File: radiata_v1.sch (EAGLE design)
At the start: 91 parts, among them IC1 TINY24/44/84-SSU, IC2 MEGA48/88/168-AU

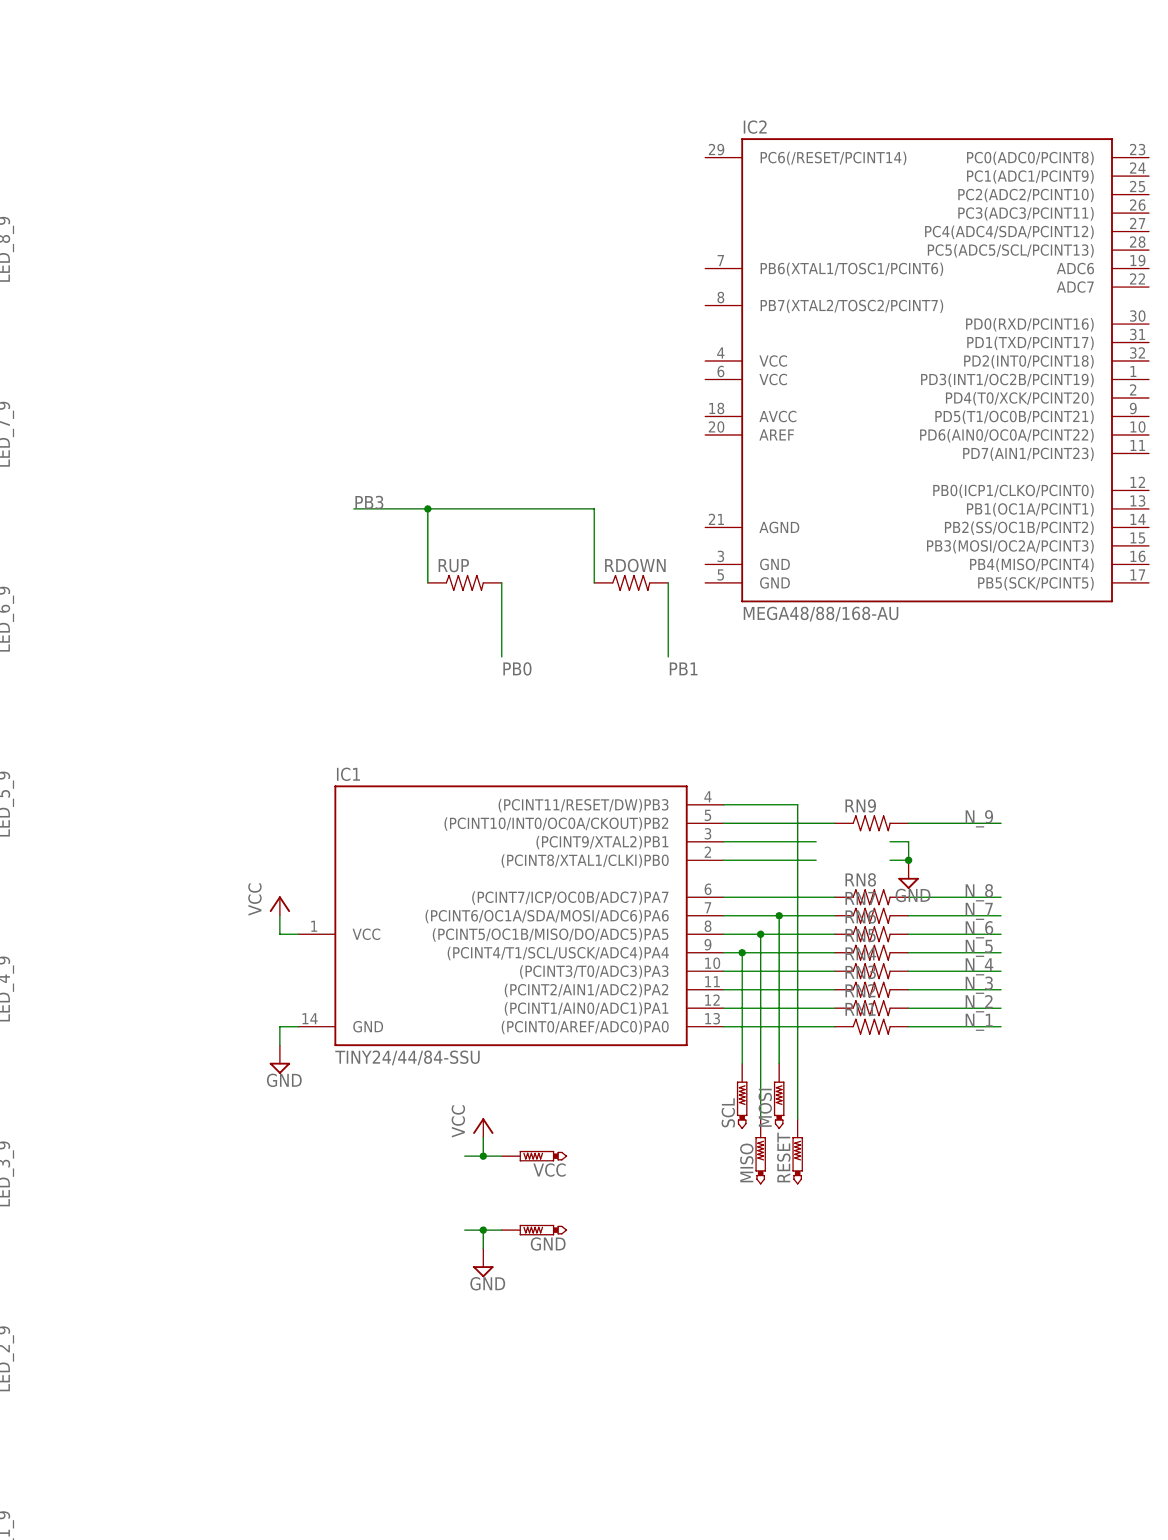
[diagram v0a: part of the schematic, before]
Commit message: rename simpleclock to 'radiata'
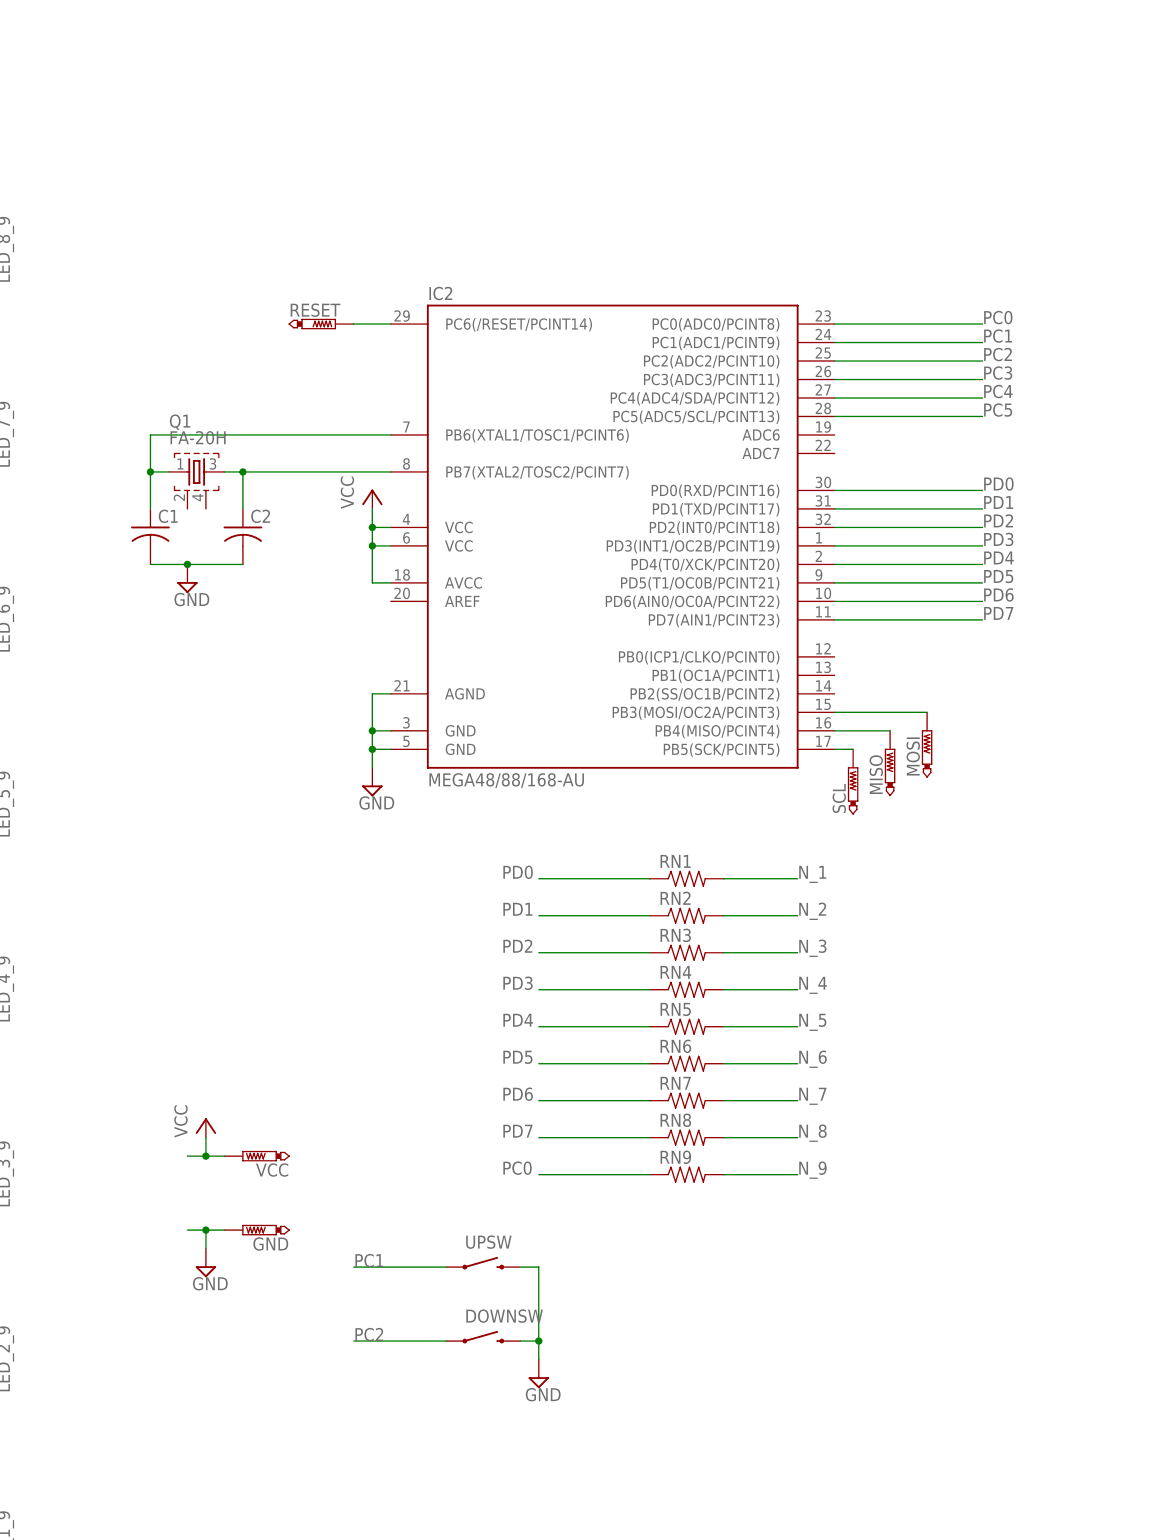
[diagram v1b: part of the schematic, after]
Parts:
- removed IC1: TINY24/44/84-SSU, avr-7:TINY24/44/84-SSU
- removed RDOWN, RUP: (no value), SparkFun:RESISTOR1206
- added C1, C2: (no value), rcl:C-USC0603
- added DOWNSW, UPSW: SWITCH-MOMENTARY-2, SparkFun:SWITCH-MOMENTARY-2
- added Q1: FA-20H, crystal:FA-20H
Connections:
- removed net PA0: IC1.(PCINT0/AREF/ADC0)PA0, RN1.1
- removed net PA1: IC1.(PCINT1/AIN0/ADC1)PA1, RN2.1
- removed net PA2: IC1.(PCINT2/AIN1/ADC2)PA2, RN3.1
- removed net PA3: IC1.(PCINT3/T0/ADC3)PA3, RN4.1
- removed net PA4: IC1.(PCINT4/T1/SCL/USCK/ADC4)PA4, RN5.1, SCL.TP
- removed net PA5: IC1.(PCINT5/OC1B/MISO/DO/ADC5)PA5, MISO.TP, RN6.1
- removed net PA6: IC1.(PCINT6/OC1A/SDA/MOSI/ADC6)PA6, MOSI.TP, RN7.1
- removed net PA7: IC1.(PCINT7/ICP/OC0B/ADC7)PA7, RN8.1
- removed net PB2: IC1.(PCINT10/INT0/OC0A/CKOUT)PB2, RN9.1
- removed net PB3: IC1.(PCINT11/RESET/DW)PB3, RDOWN.1, RESET.TP, RUP.1
- new net N$5: IC2.PC6(/RESET/PCINT14), RESET.TP
- new net N$6: IC2.PB5(SCK/PCINT5), SCL.TP
- new net N$7: IC2.PB4(MISO/PCINT4), MISO.TP
- new net N$8: IC2.PB3(MOSI/OC2A/PCINT3), MOSI.TP
- new net PC0: IC2.PC0(ADC0/PCINT8), RN9.1
- new net PC1: IC2.PC1(ADC1/PCINT9), UPSW.1
- new net PC2: DOWNSW.1, IC2.PC2(ADC2/PCINT10)
- new net PC3: IC2.PC3(ADC3/PCINT11)
- new net PC4: IC2.PC4(ADC4/SDA/PCINT12)
- new net PC5: IC2.PC5(ADC5/SCL/PCINT13)
- new net PD0: IC2.PD0(RXD/PCINT16), RN1.1
- new net PD1: IC2.PD1(TXD/PCINT17), RN2.1
- new net PD2: IC2.PD2(INT0/PCINT18), RN3.1
- new net PD3: IC2.PD3(INT1/OC2B/PCINT19), RN4.1
- new net PD4: IC2.PD4(T0/XCK/PCINT20), RN5.1
- new net PD5: IC2.PD5(T1/OC0B/PCINT21), RN6.1
- new net PD6: IC2.PD6(AIN0/OC0A/PCINT22), RN7.1
- new net PD7: IC2.PD7(AIN1/PCINT23), RN8.1
- net GND: now also C1.2, C2.2, DOWNSW.2, IC2.AGND, IC2.GND@1, IC2.GND@2, UPSW.2; no longer IC1.GND
- net PB0: now also C2.1, IC2.PB7(XTAL2/TOSC2/PCINT7), Q1.3; no longer IC1.(PCINT8/XTAL1/CLKI)PB0, RUP.2
- net PB1: now also C1.1, IC2.PB6(XTAL1/TOSC1/PCINT6), Q1.1; no longer IC1.(PCINT9/XTAL2)PB1, RDOWN.2
- net VCC: now also IC2.AVCC, IC2.VCC@1, IC2.VCC@2; no longer IC1.VCC
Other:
- moved on the sheet: GND, IC2, MISO, MOSI, RESET, RN1, RN2, RN3, RN4, RN5, RN6, RN7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

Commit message: lots of progress, driving towards a scroll wheel that passes DRC
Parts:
- added GND2, V+: PTR1TP20SQ, testpad:PTR1TP20SQ
- added RR1, RR2, RR3, RS1, RS2, RS3: (no value), SparkFun:RESISTOR1206
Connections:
- new net ROTOR1: RR1.1, RS1.2
- new net ROTOR2: RR2.1, RS2.2
- new net ROTOR3: RR3.1, RS3.2
- net GND: now also GND2.TP
- net PC2: now also RS1.1, RS2.1, RS3.1
- net PC3: now also RR1.2
- net PC4: now also RR2.2
- net PC5: now also RR3.2
- net VCC: now also V+.TP
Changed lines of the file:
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@@
 <part name="DOWNSW" library="SparkFun" deviceset="SWITCH-MOMENTARY-2" device=""/>
 <part name="SUPPLY5" library="supply2" deviceset="GND" device=""/>
+<part name="RS1" library="SparkFun" deviceset="RESISTOR" device="1206"/>
+<part name="RS2" library="SparkFun" deviceset="RESISTOR" device="1206"/>
+<part name="RS3" library="SparkFun" deviceset="RESISTOR" device="1206"/>
+<part name="RR1" library="SparkFun" deviceset="RESISTOR" device="1206"/>
+<part name="RR2" library="SparkFun" deviceset="RESISTOR" device="1206"/>
+<part name="RR3" library="SparkFun" deviceset="RESISTOR" device="1206"/>
+<part name="GND2" library="testpad" deviceset="PTR1" device="TP20SQ"/>
+<part name="V+" library="testpad" deviceset="PTR1" device="TP20SQ"/>
 </parts>
 <sheets>
@@
 </instance>
 <instance part="SUPPLY5" gate="GND" x="304.8" y="48.26"/>
+<instance part="RS1" gate="G$1" x="299.72" y="30.48"/>
+<instance part="RS2" gate="G$1" x="299.72" y="22.86"/>
+<instance part="RS3" gate="G$1" x="299.72" y="15.24"/>
+<instance part="RR1" gate="G$1" x="317.5" y="30.48"/>
+<instance part="RR2" gate="G$1" x="317.5" y="22.86"/>
+<instance part="RR3" gate="G$1" x="317.5" y="15.24"/>
+<instance part="GND2" gate="G$1" x="254" y="68.58" rot="R270"/>
+<instance part="V+" gate="G$1" x="254" y="78.74" rot="R270"/>
 </instances>
 <busses>
@@
 <wire x1="256.54" y1="78.74" x2="259.08" y2="78.74" width="0.1524" layer="91"/>
 <junction x="259.08" y="78.74"/>
+<pinref part="V+" gate="G$1" pin="TP"/>
 </segment>
 <segment>
@@
 <wire x1="259.08" y1="66.04" x2="259.08" y2="68.58" width="0.1524" layer="91"/>
 <junction x="259.08" y="68.58"/>
+<pinref part="GND2" gate="G$1" pin="TP"/>
 </segment>
 <segment>
@@
 <label x="279.4" y="53.34" size="1.778" layer="95"/>
 </segment>
+<segment>
+<pinref part="RS3" gate="G$1" pin="1"/>
+<wire x1="294.64" y1="15.24" x2="292.1" y2="15.24" width="0.1524" layer="91"/>
+<wire x1="292.1" y1="15.24" x2="292.1" y2="22.86" width="0.1524" layer="91"/>
+<wire x1="292.1" y1="22.86" x2="292.1" y2="30.48" width="0.1524" layer="91"/>
+<wire x1="292.1" y1="30.48" x2="279.4" y2="30.48" width="0.1524" layer="91"/>
+<pinref part="RS1" gate="G$1" pin="1"/>
+<wire x1="294.64" y1="30.48" x2="292.1" y2="30.48" width="0.1524" layer="91"/>
+<junction x="292.1" y="30.48"/>
+<pinref part="RS2" gate="G$1" pin="1"/>
+<wire x1="294.64" y1="22.86" x2="292.1" y2="22.86" width="0.1524" layer="91"/>
+<junction x="292.1" y="22.86"/>
+<label x="279.4" y="30.48" size="1.778" layer="95"/>
+</segment>
 </net>
 <net name="PC3" class="0">
@@
 <label x="365.76" y="185.42" size="1.778" layer="95"/>
 </segment>
+<segment>
+<pinref part="RR1" gate="G$1" pin="2"/>
+<wire x1="332.74" y1="30.48" x2="322.58" y2="30.48" width="0.1524" layer="91"/>
+<label x="332.74" y="30.48" size="1.778" layer="95"/>
+</segment>
 </net>
 <net name="PC4" class="0">
@@
 <label x="365.76" y="182.88" size="1.778" layer="95"/>
 </segment>
+<segment>
+<pinref part="RR2" gate="G$1" pin="2"/>
+<wire x1="332.74" y1="22.86" x2="322.58" y2="22.86" width="0.1524" layer="91"/>
+<label x="332.74" y="22.86" size="1.778" layer="95"/>
+</segment>
 </net>
 <net name="PC5" class="0">
@@
 <label x="365.76" y="180.34" size="1.778" layer="95"/>
 </segment>
-</net>
+<segment>
+<pinref part="RR3" gate="G$1" pin="2"/>
+<wire x1="332.74" y1="15.24" x2="322.58" y2="15.24" width="0.1524" layer="91"/>
+<label x="332.74" y="15.24" size="1.778" layer="95"/>
+</segment>
+</net>
+<net name="ROTOR1" class="0">
+<segment>
+<pinref part="RS1" gate="G$1" pin="2"/>
+<pinref part="RR1" gate="G$1" pin="1"/>
+<wire x1="304.8" y1="30.48" x2="312.42" y2="30.48" width="0.1524" layer="91"/>
+<label x="302.26" y="33.02" size="1.778" layer="95"/>
+</segment>
+</net>
+<net name="ROTOR2" class="0">
+<segment>
+<pinref part="RS2" gate="G$1" pin="2"/>
+<pinref part="RR2" gate="G$1" pin="1"/>
+<wire x1="304.8" y1="22.86" x2="312.42" y2="22.86" width="0.1524" layer="91"/>
+<label x="302.26" y="25.4" size="1.778" layer="95"/>
+</segment>
+</net>
+<net name="ROTOR3" class="0">
+<segment>
+<pinref part="RS3" gate="G$1" pin="2"/>
+<pinref part="RR3" gate="G$1" pin="1"/>
+<wire x1="304.8" y1="15.24" x2="312.42" y2="15.24" width="0.1524" layer="91"/>
+<label x="302.26" y="17.78" size="1.778" layer="95"/>
+</segment>
+</net>

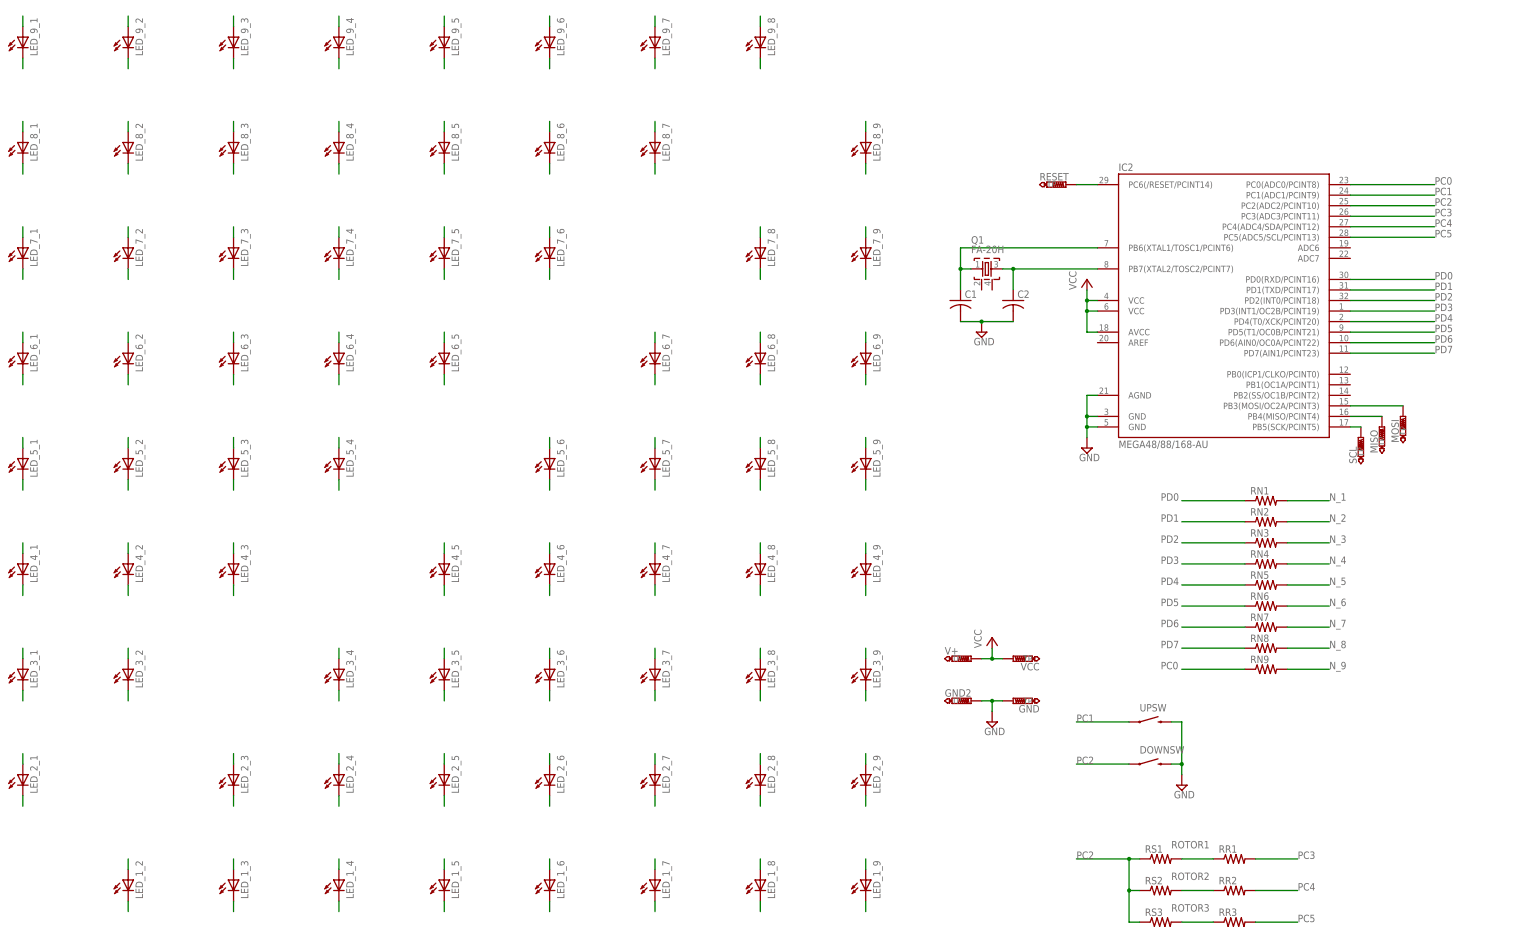
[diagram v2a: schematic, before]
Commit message: add push/pull resistors
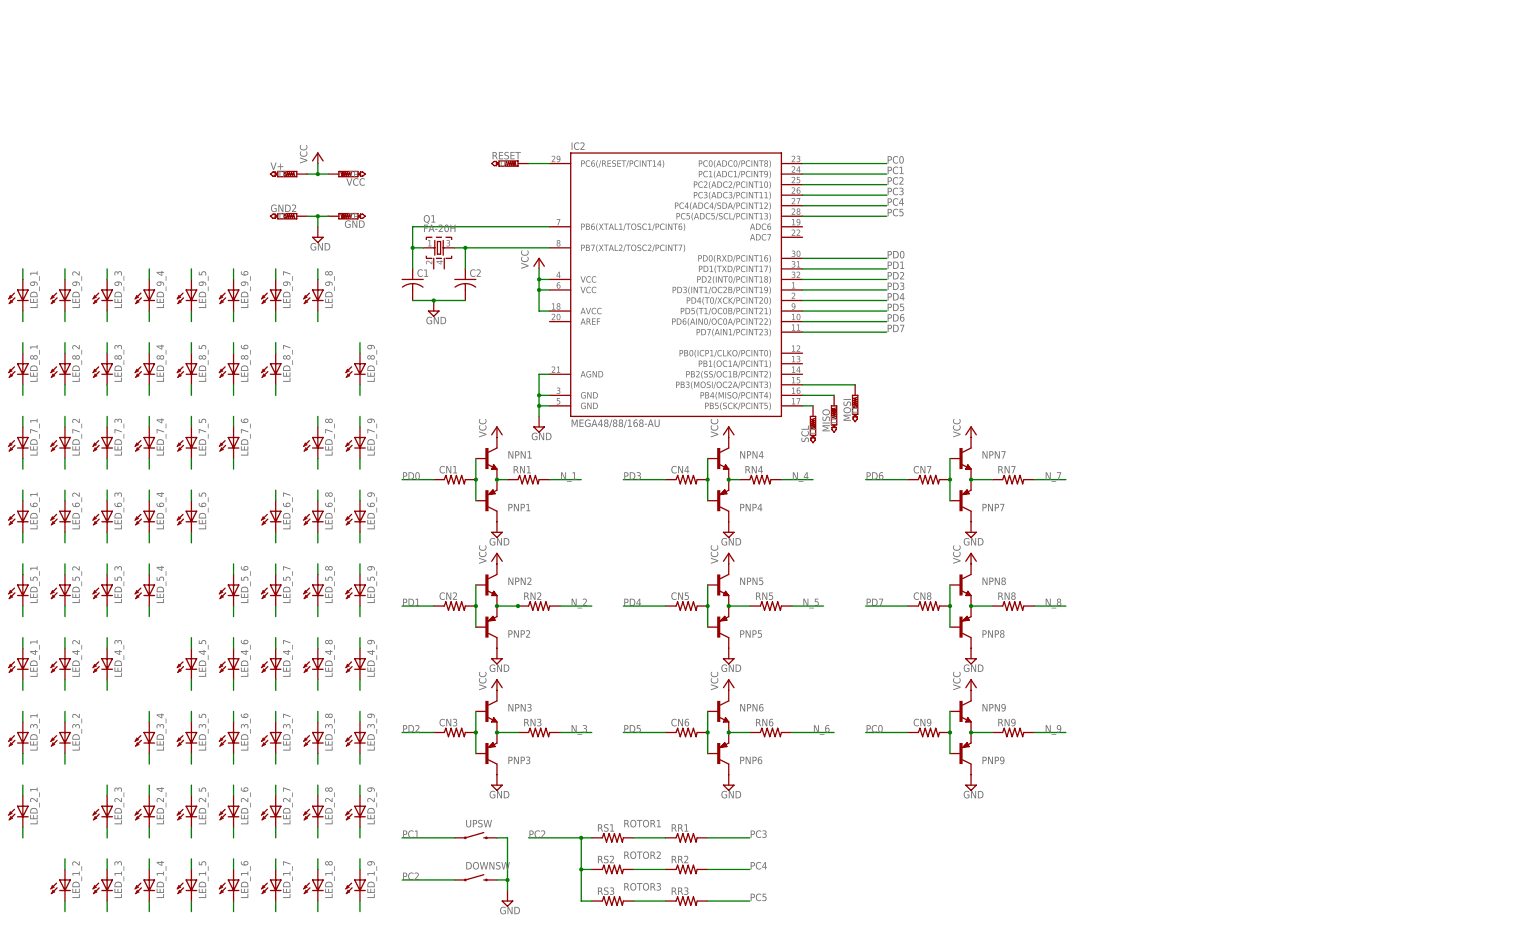
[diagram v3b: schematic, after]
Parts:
- added CN1, CN2, CN3, CN4, CN5, CN6, CN7, CN8, CN9: (no value), rcl:R-US_M0805
- added NPN1, NPN2, NPN3, NPN4, NPN5, NPN6, NPN7, NPN8, NPN9: (no value), transistor:MMBT2222ALT1-NPN-SOT23-BEC
- added PNP1, PNP2, PNP3, PNP4, PNP5, PNP6, PNP7, PNP8, PNP9: (no value), transistor:MMBT540LT1-PNP-SOT23-BEC
- GND, MISO, MOSI, RESET, SCL, VCC: value PTR1PAD1-13 -> PTR1TP19R; device testpad:PTR1PAD1-13 -> testpad:PTR1TP19R
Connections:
- new net N$10: CN1.2, NPN1.B, PNP1.B
- new net N$11: NPN2.E, PNP2.E, RN2.1
- new net N$12: CN2.2, NPN2.B, PNP2.B
- new net N$13: NPN3.E, PNP3.E, RN3.1
- new net N$14: CN3.2, NPN3.B, PNP3.B
- new net N$15: NPN4.E, PNP4.E, RN4.1
- new net N$16: CN4.2, NPN4.B, PNP4.B
- new net N$17: NPN5.E, PNP5.E, RN5.1
- new net N$18: CN5.2, NPN5.B, PNP5.B
- new net N$19: NPN6.E, PNP6.E, RN6.1
- new net N$20: CN6.2, NPN6.B, PNP6.B
- new net N$24: NPN7.E, PNP7.E, RN7.1
- new net N$25: CN7.2, NPN7.B, PNP7.B
- new net N$26: NPN8.E, PNP8.E, RN8.1
- new net N$27: CN8.2, NPN8.B, PNP8.B
- new net N$28: NPN9.E, PNP9.E, RN9.1
- new net N$29: CN9.2, NPN9.B, PNP9.B
- new net N$9: NPN1.E, PNP1.E, RN1.1
- net GND: now also PNP1.C, PNP2.C, PNP3.C, PNP4.C, PNP5.C, PNP6.C, PNP7.C, PNP8.C, PNP9.C
- net PC0: now also CN9.1; no longer RN9.1
- net PD0: now also CN1.1; no longer RN1.1
- net PD1: now also CN2.1; no longer RN2.1
- net PD2: now also CN3.1; no longer RN3.1
- net PD3: now also CN4.1; no longer RN4.1
- net PD4: now also CN5.1; no longer RN5.1
- net PD5: now also CN6.1; no longer RN6.1
- net PD6: now also CN7.1; no longer RN7.1
- net PD7: now also CN8.1; no longer RN8.1
- net VCC: now also NPN1.C, NPN2.C, NPN3.C, NPN4.C, NPN5.C, NPN6.C, NPN7.C, NPN8.C, NPN9.C
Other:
- moved on the sheet: C1, C2, DOWNSW, GND, GND2, IC2, LED_1_2, LED_1_3, LED_1_4, LED_1_5, LED_1_6, LED_1_7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
